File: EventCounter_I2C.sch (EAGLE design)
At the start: 37 parts, among them J1 CONN_42.54_SCREW, J2 CONN_32.54_SCREW, Q1 DMG3404, Q2 FDN360P, Q3 2N7002, U10 TXS0102DQM, U11 TPS7A0533DBV, U4 TLV3691DCK, U7 SN74AUP1G34SC70, U8 SN74AUP3G34DCU, U9 ATTINY441/841VQFN

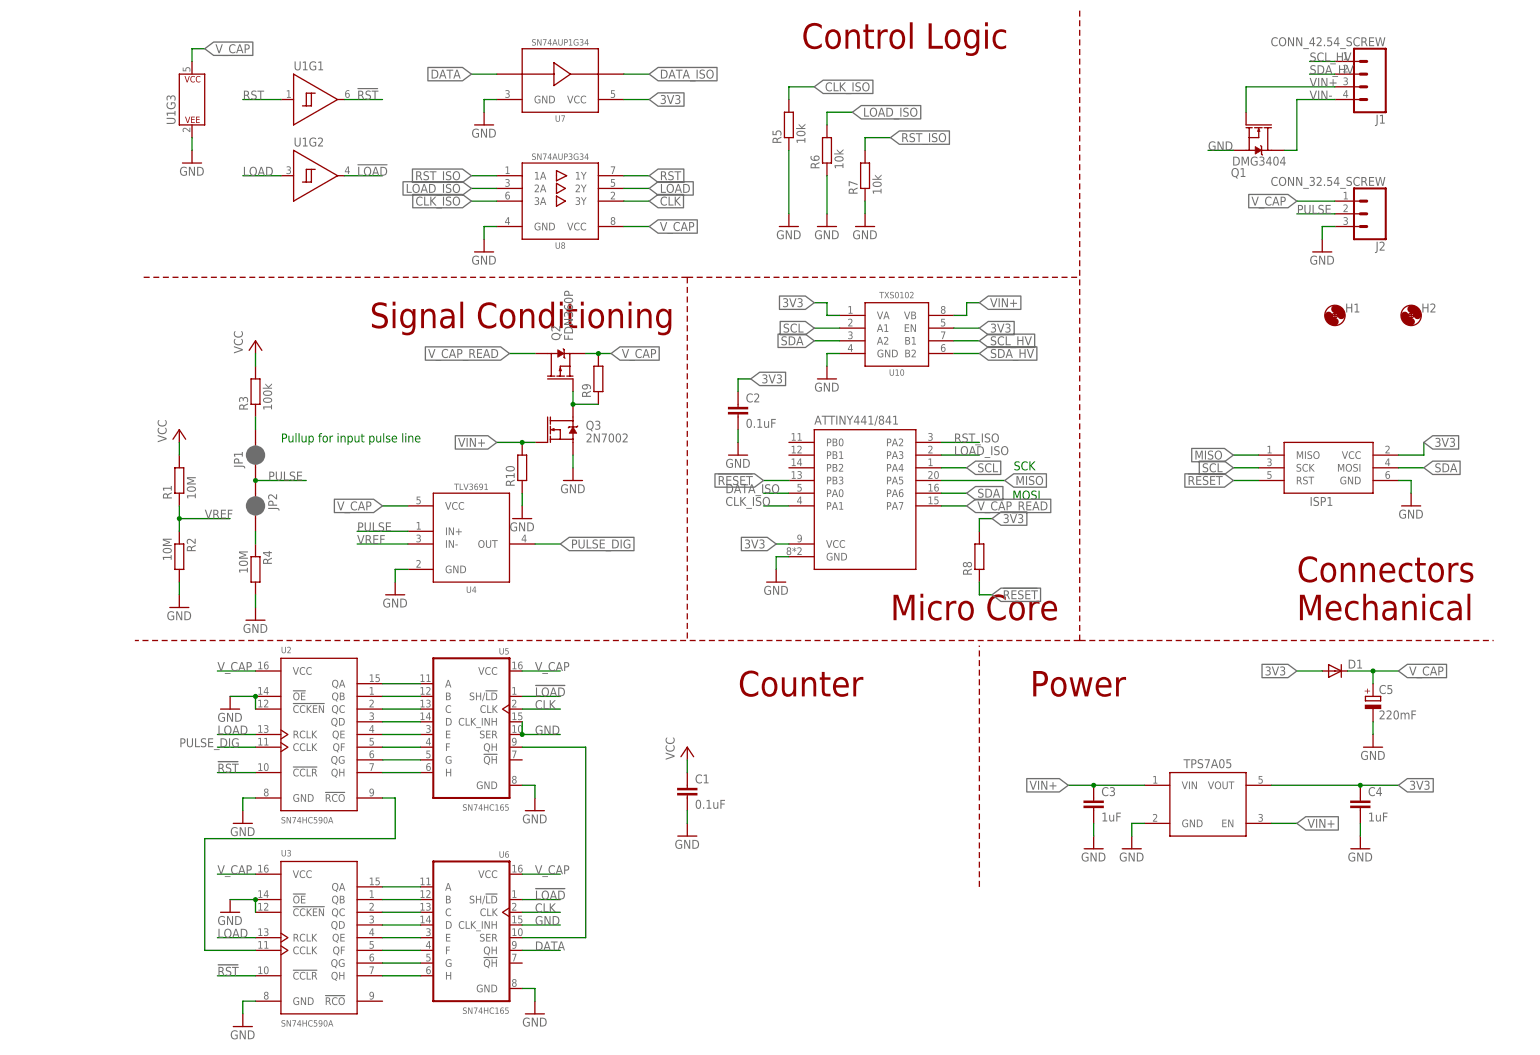
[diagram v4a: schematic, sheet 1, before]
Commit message: Routing and design update for v1.1
Cleanup/verification required before sending to fab
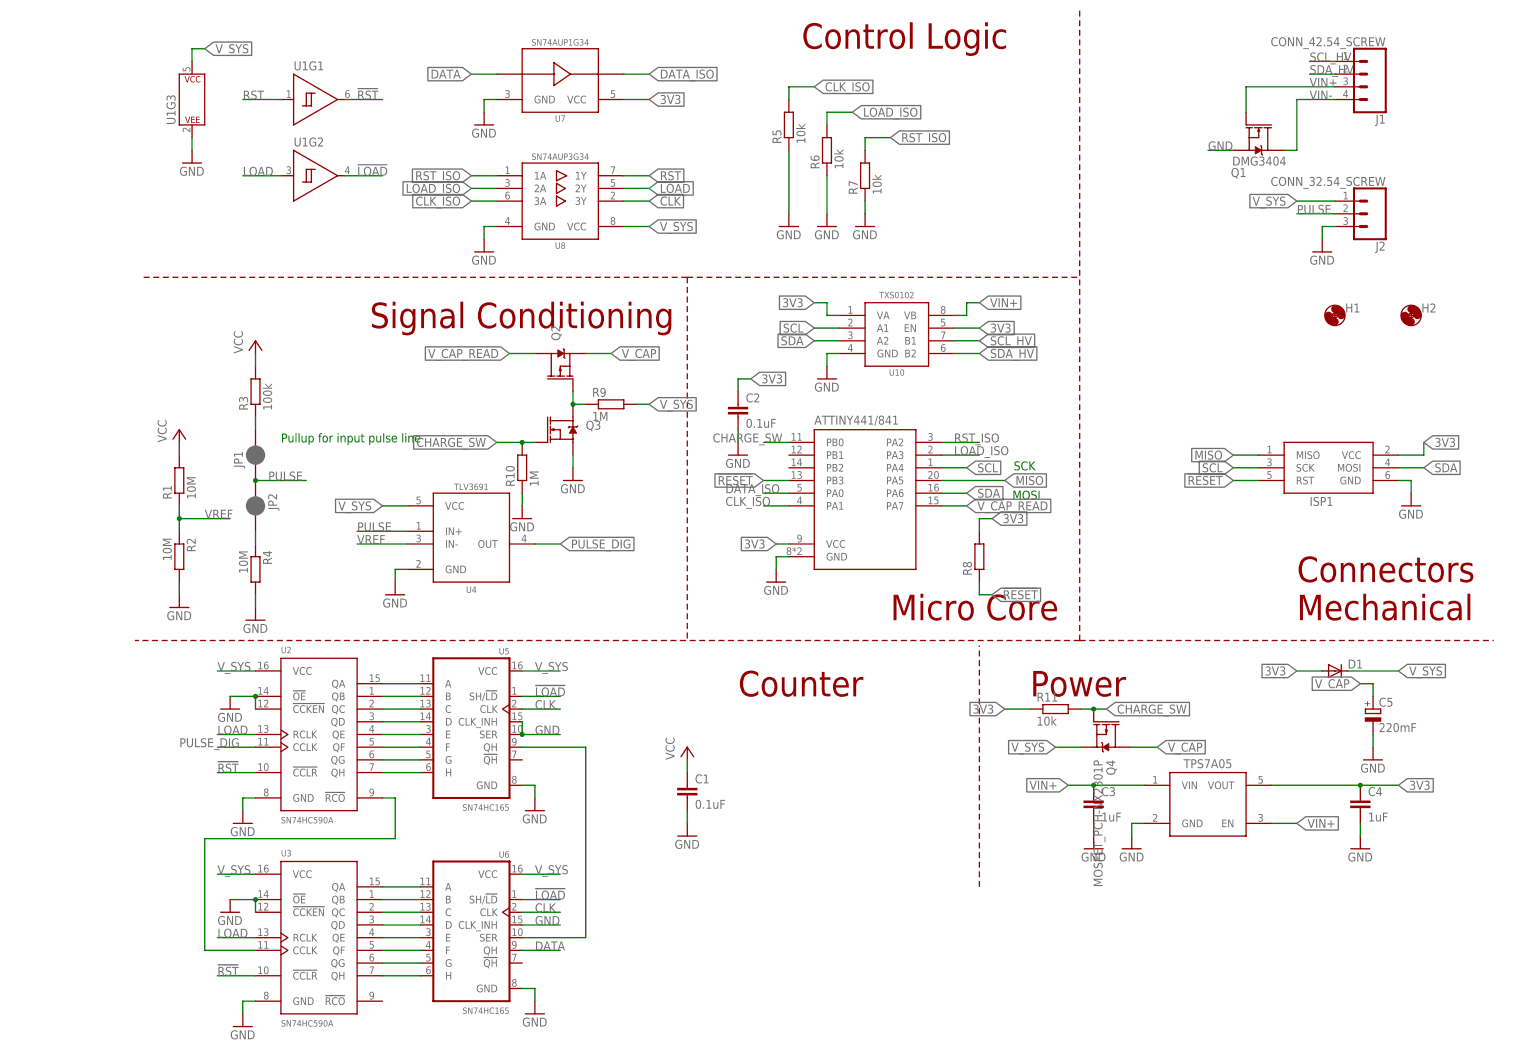
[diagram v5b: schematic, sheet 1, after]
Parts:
- added Q4: MOSFET_PCH-NX2301P, bschulz:MOSFET_PCH-NX2301P
- added R11: 10k, bschulz_passives:R-EU_10KR0402
- C5: DIGIKEY (none) -> 604-1020-1-ND; MF (none) -> Elna; MPN (none) -> DSK-3R3H224U-HL
- D1: DIGIKEY (none) -> BAT43W-FDICT-ND; MF (none) -> Diodes Incorporated; MPN (none) -> BAT43W-7-F
- Q2: value FDN360P -> MOSFET_PCH-RZM001P02; device bschulz:MOSFET_PCH-FDN360P -> bschulz:MOSFET_PCH-RZM001P02
- Q3: value 2N7002 -> MOSFET-NCH-RE1C002UN; device bschulz:MOSFET-NCH-2N7002PW -> bschulz:MOSFET-NCH-RE1C002UN
- R10, R9: value (none) -> 1M; device bschulz_passives:R-EU_R0402 -> bschulz_passives:R-EU_1MR0402
- R3: device bschulz_passives:R-EU_R0603 -> bschulz_passives:R-EU_100KR0603
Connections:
- new net CHARGE_SW: Q3.G, Q4.G, R10.2, R11.2, U9.PB0
- new net V_SYS: C1.1, D1.C, J2.1, Q4.S, R1.2, R3.2, R9.2, U1G3.P$V+, U2.VCC, U3.VCC, U4.VCC, U5.VCC, U6.VCC, U8.VCC
- net 3V3: now also R11.1
- net VIN+: no longer Q3.G, R10.2
- net V_CAP: now also Q4.D; no longer C1.1, D1.C, J2.1, R1.2, R3.2, R9.2, U1G3.P$V+, U2.VCC, U3.VCC, U4.VCC, U5.VCC, U6.VCC, U8.VCC
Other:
- moved on the sheet: C5, R9

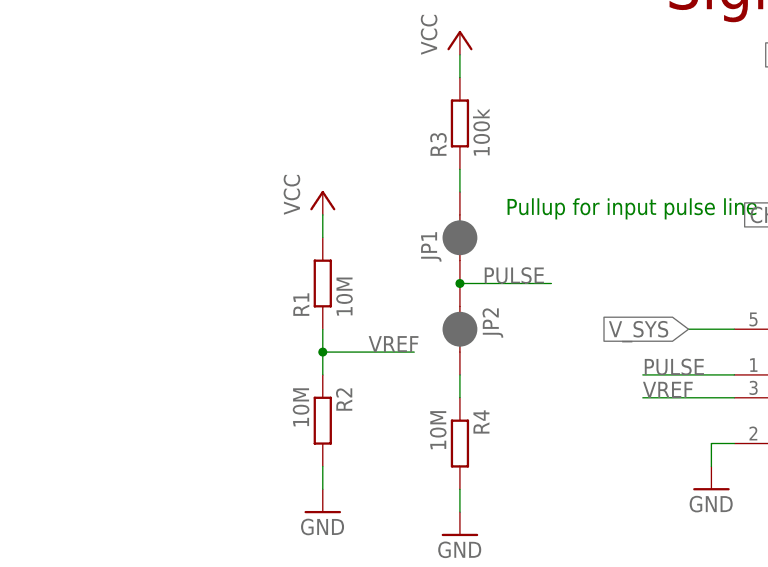
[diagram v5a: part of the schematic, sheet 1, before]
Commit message: Minor cleanup, generated gerbers, sent v1.1 to fab
Minor cleanup and rearranging silkscreen names, changed jumper configuration
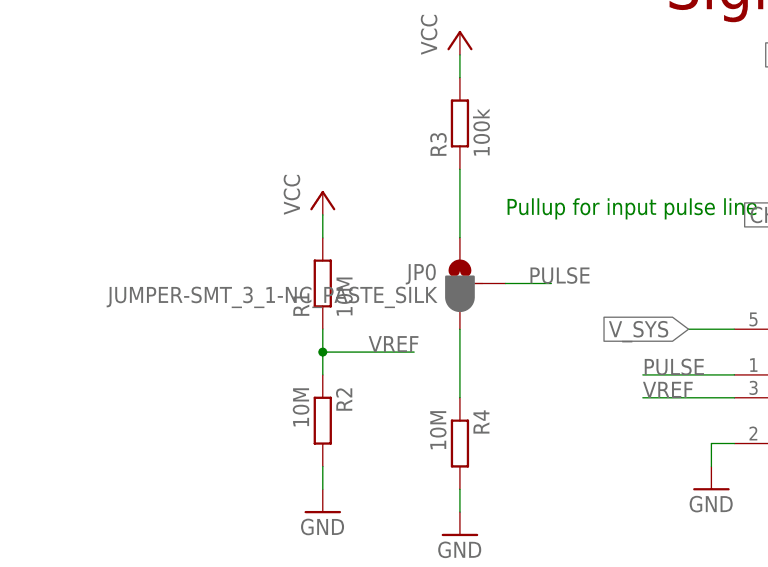
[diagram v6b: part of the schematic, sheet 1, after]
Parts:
- removed JP1, JP2: JUMPER-SMT_2_NC_PASTE_SILK, SparkFun-Jumpers:JUMPER-SMT_2_NC_PASTE_SILK
- added JP0: JUMPER-SMT_3_1-NC_PASTE_SILK, SparkFun-Jumpers:JUMPER-SMT_3_1-NC_PASTE_SILK
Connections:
- net N$19: now also JP0.3; no longer JP2.2
- net N$20: now also JP0.1; no longer JP1.2
- net PULSE: now also JP0.2; no longer JP1.1, JP2.1
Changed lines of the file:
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@@
 <part name="J1" library="bschulz" deviceset="CONN_4" device="2.54_SCREW"/>
 <part name="Q1" library="bschulz" deviceset="MOSFET-NCH" device="-DMG3404L" value="DMG3404"/>
-<part name="JP1" library="SparkFun-Jumpers" library_urn="urn:adsk.eagle:library:528" deviceset="JUMPER-SMT_2_NC_PASTE" device="_SILK" package3d_urn="urn:adsk.eagle:package:39282/1"/>
 <part name="R3" library="bschulz_passives" deviceset="R-EU_" device="R0603" technology="100K" value="100k"/>
 <part name="P+2" library="supply1" library_urn="urn:adsk.eagle:library:371" deviceset="VCC" device=""/>
@@
 <part name="GND8" library="supply1" library_urn="urn:adsk.eagle:library:371" deviceset="GND" device=""/>
 <part name="R4" library="bschulz_passives" deviceset="R-EU_" device="R0603" technology="10M" value="10M"/>
-<part name="JP2" library="SparkFun-Jumpers" library_urn="urn:adsk.eagle:library:528" deviceset="JUMPER-SMT_2_NC_PASTE" device="_SILK" package3d_urn="urn:adsk.eagle:package:39282/1"/>
 <part name="GND7" library="supply1" library_urn="urn:adsk.eagle:library:371" deviceset="GND" device=""/>
 <part name="U11" library="bschulz" deviceset="TPS7A05*" device="DBV" technology="33"/>
@@
 <part name="Q4" library="bschulz" deviceset="MOSFET_PCH" device="-NX2301P"/>
 <part name="R11" library="bschulz_passives" deviceset="R-EU_" device="R0402" technology="10K" value="10k"/>
+<part name="JP0" library="SparkFun-Jumpers" library_urn="urn:adsk.eagle:library:528" deviceset="JUMPER-SMT_3_1-NC_PASTE" device="_SILK" package3d_urn="urn:adsk.eagle:package:39293/1"/>
 </parts>
 <sheets>
@@
 <attribute name="VALUE" x="223.266" y="179.832" size="1.778" layer="96" font="vector"/>
 </instance>
-<instance part="JP1" gate="G$1" x="27.94" y="121.92" smashed="yes" rot="R90">
-<attribute name="NAME" x="25.4" y="119.38" size="1.778" layer="95" font="vector" rot="R90"/>
-</instance>
 <instance part="R3" gate="G$1" x="27.94" y="134.62" smashed="yes" rot="R90">
 <attribute name="NAME" x="26.4414" y="130.81" size="1.778" layer="95" rot="R90"/>
@@
 <attribute name="VALUE" x="24.638" y="102.87" size="1.778" layer="96" rot="R270"/>
 </instance>
-<instance part="JP2" gate="G$1" x="27.94" y="111.76" smashed="yes" rot="R270">
-<attribute name="NAME" x="30.48" y="114.3" size="1.778" layer="95" font="vector" rot="R270"/>
-</instance>
 <instance part="GND7" gate="1" x="27.94" y="88.9" smashed="yes">
 <attribute name="VALUE" x="25.4" y="86.36" size="1.778" layer="96"/>
@@
 <attribute name="NAME" x="184.15" y="72.6186" size="1.778" layer="95"/>
 <attribute name="VALUE" x="184.15" y="67.818" size="1.778" layer="96"/>
+</instance>
+<instance part="JP0" gate="G$1" x="27.94" y="116.84" smashed="yes" rot="MR0">
+<attribute name="NAME" x="25.4" y="117.221" size="1.778" layer="95" font="vector" rot="MR0"/>
+<attribute name="VALUE" x="25.4" y="116.459" size="1.778" layer="96" font="vector" rot="MR0" align="top-left"/>
 </instance>
 </instances>
@@
 <net name="PULSE" class="0">
 <segment>
-<pinref part="JP1" gate="G$1" pin="1"/>
-<wire x1="27.94" y1="116.84" x2="38.1" y2="116.84" width="0.1524" layer="91"/>
-<label x="30.48" y="116.84" size="1.778" layer="95" ratio="15"/>
-<pinref part="JP2" gate="G$1" pin="1"/>
-<junction x="27.94" y="116.84"/>
+<wire x1="33.02" y1="116.84" x2="38.1" y2="116.84" width="0.1524" layer="91"/>
+<label x="35.56" y="116.84" size="1.778" layer="95" ratio="15"/>
+<pinref part="JP0" gate="G$1" pin="2"/>
 </segment>
 <segment>
@@
 <net name="N$20" class="0">
 <segment>
-<pinref part="JP1" gate="G$1" pin="2"/>
-<wire x1="27.94" y1="127" x2="27.94" y2="129.54" width="0.1524" layer="91"/>
 <pinref part="R3" gate="G$1" pin="1"/>
+<pinref part="JP0" gate="G$1" pin="1"/>
+<wire x1="27.94" y1="121.92" x2="27.94" y2="129.54" width="0.1524" layer="91"/>
 </segment>
 </net>
@@
 <segment>
 <pinref part="R4" gate="G$1" pin="1"/>
-<pinref part="JP2" gate="G$1" pin="2"/>
-<wire x1="27.94" y1="104.14" x2="27.94" y2="106.68" width="0.1524" layer="91"/>
-</segment>
-</net>
+<pinref part="JP0" gate="G$1" pin="3"/>
+<wire x1="27.94" y1="111.76" x2="27.94" y2="104.14" width="0.1524" layer="91"/>
+</segment>
+</net>

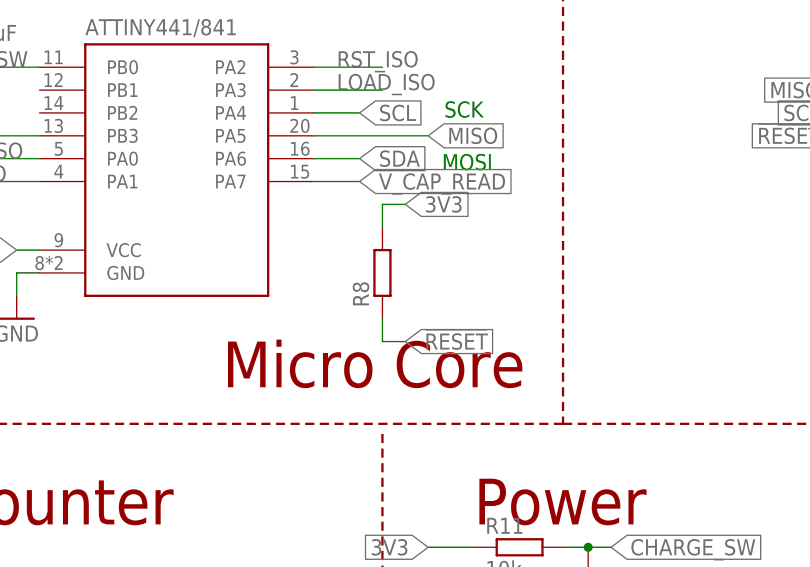
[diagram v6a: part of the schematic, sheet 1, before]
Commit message: Minor value updates
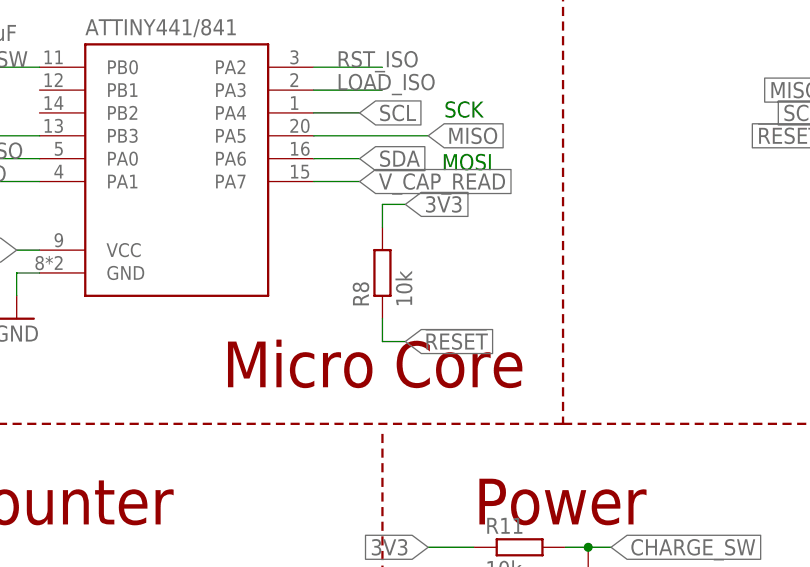
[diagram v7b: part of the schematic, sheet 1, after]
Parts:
- R8: value (none) -> 10k
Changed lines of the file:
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@@
 <part name="U1" library="bschulz" deviceset="SN74*2G14" device="SC70" technology="AUP"/>
 <part name="GND2" library="supply1" library_urn="urn:adsk.eagle:library:371" deviceset="GND" device=""/>
-<part name="R8" library="bschulz_passives" deviceset="R-EU_" device="R0402" technology="10K"/>
+<part name="R8" library="bschulz_passives" deviceset="R-EU_" device="R0402" technology="10K" value="10k"/>
 <part name="Q2" library="bschulz" deviceset="MOSFET_PCH" device="-RZM001P02" value="MOSFET_PCH-RZM001P02"/>
 <part name="Q3" library="bschulz" deviceset="MOSFET-NCH" device="-RE1C002UN" value="MOSFET-NCH-RE1C002UN"/>

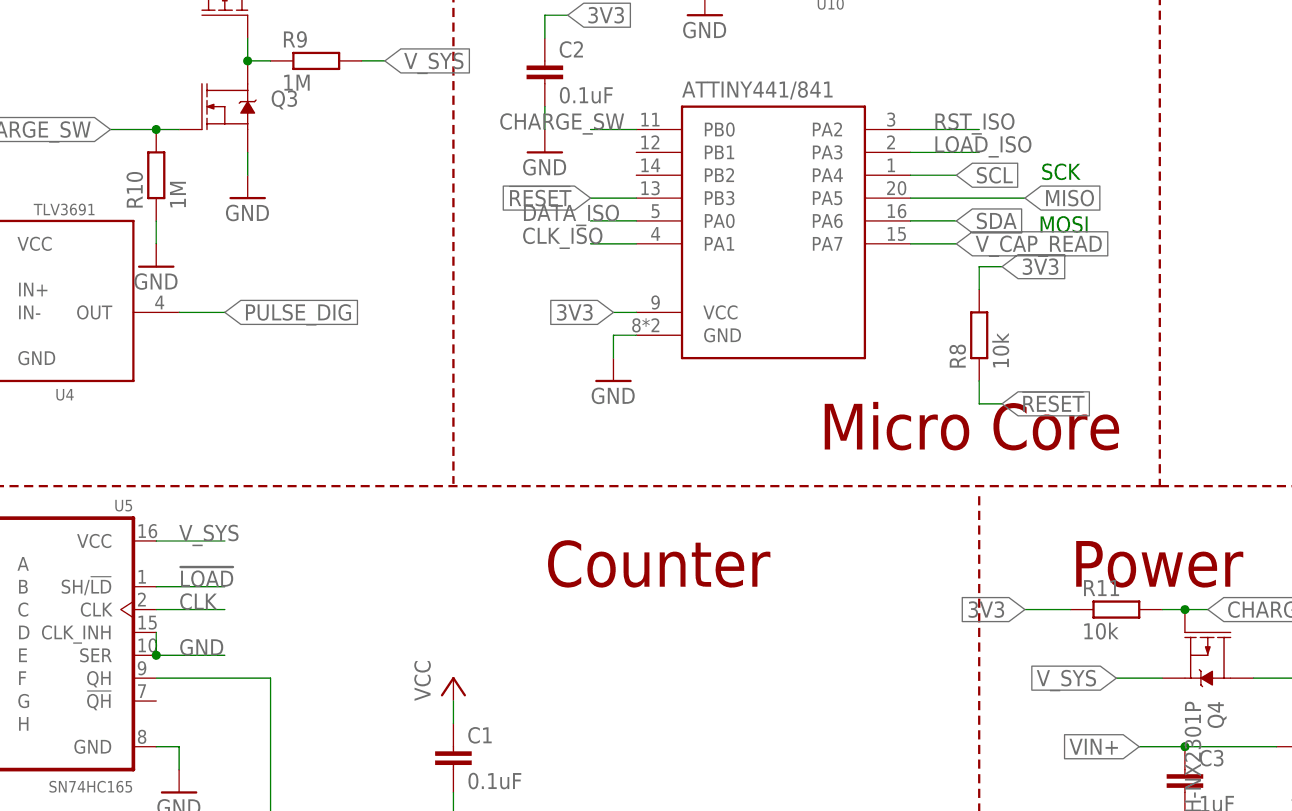
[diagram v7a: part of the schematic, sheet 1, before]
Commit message: Updated part values
Switched values of `R10` and `R11`, values were erroneously switched which resulted in the capacitor being connected to the ADC input during sleep/off state, causing significant power draw
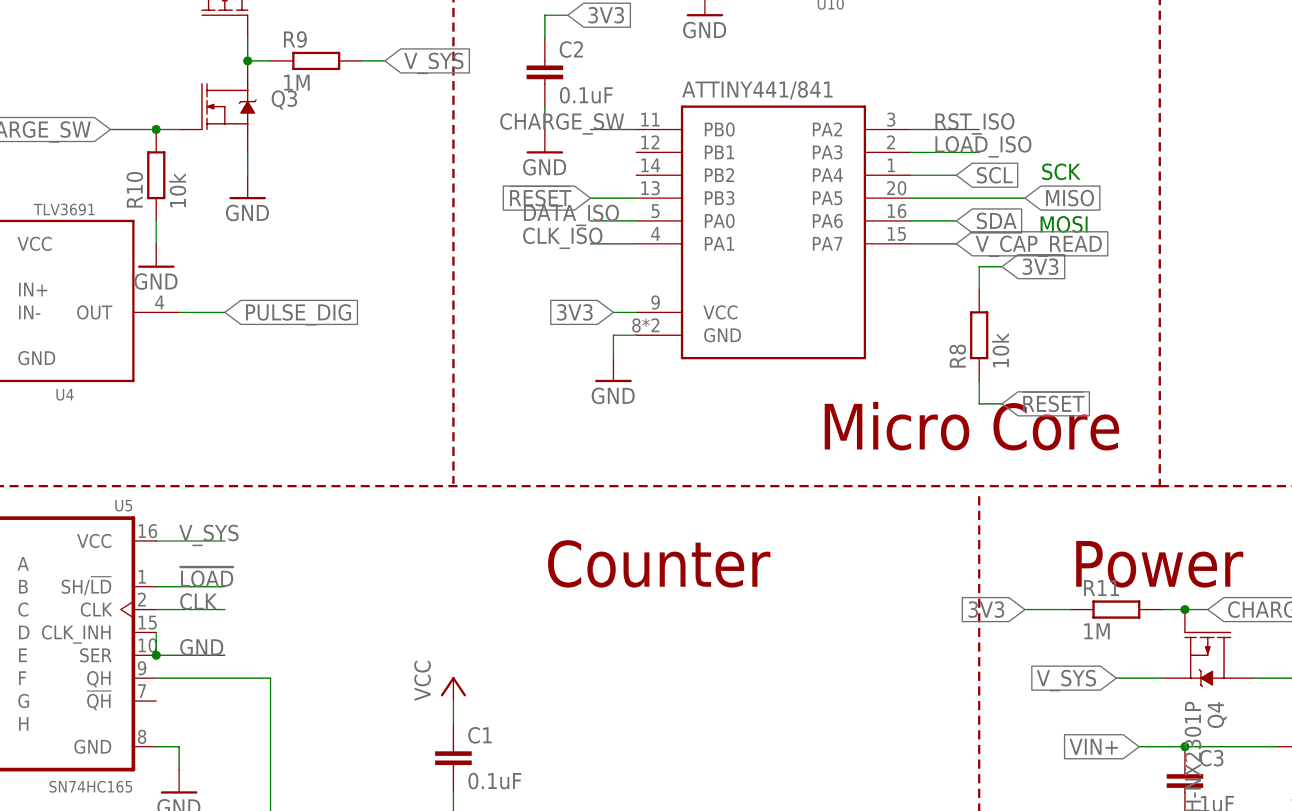
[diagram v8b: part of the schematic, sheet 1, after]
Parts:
- R10: value 1M -> 10k; device bschulz_passives:R-EU_1MR0402 -> bschulz_passives:R-EU_10KR0402
- R11: value 10k -> 1M; device bschulz_passives:R-EU_10KR0402 -> bschulz_passives:R-EU_1MR0402
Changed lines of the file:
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@@
 <part name="R9" library="bschulz_passives" deviceset="R-EU_" device="R0402" technology="1M" value="1M"/>
 <part name="GND26" library="supply1" library_urn="urn:adsk.eagle:library:371" deviceset="GND" device=""/>
-<part name="R10" library="bschulz_passives" deviceset="R-EU_" device="R0402" technology="1M" value="1M"/>
+<part name="R10" library="bschulz_passives" deviceset="R-EU_" device="R0402" technology="10K" value="10k"/>
 <part name="GND27" library="supply1" library_urn="urn:adsk.eagle:library:371" deviceset="GND" device=""/>
 <part name="Q4" library="bschulz" deviceset="MOSFET_PCH" device="-NX2301P"/>
-<part name="R11" library="bschulz_passives" deviceset="R-EU_" device="R0402" technology="10K" value="10k"/>
+<part name="R11" library="bschulz_passives" deviceset="R-EU_" device="R0402" technology="1M" value="1M"/>
 <part name="JP0" library="SparkFun-Jumpers" library_urn="urn:adsk.eagle:library:528" deviceset="JUMPER-SMT_3_1-NC_PASTE" device="_SILK" package3d_urn="urn:adsk.eagle:package:39293/1"/>
 </parts>
